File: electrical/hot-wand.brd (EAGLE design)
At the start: 112 x 72 mm, 188 parts, among them IC1 12V R-78K12-2.0, IC2 3V3 R-78K3.3, Q1 STP19NF20, Q2 IRF510, Q3 BC846B, Q4 SIRS5800DP-T1-GE3, Q5 2N7002K, Q6 DMTH64M2LPDWQ-13, Q7 G3404, U1 TPS54560DDA, U2 1EDN8511BXUSA1, U3 INA138, U4 LM74700QDBVTQ1, U5 AP53781, U6 SSD1306-4PIN-0.91N-VERT, U7 STM32F030F4P6, Y1 27.12 MHz 10pF

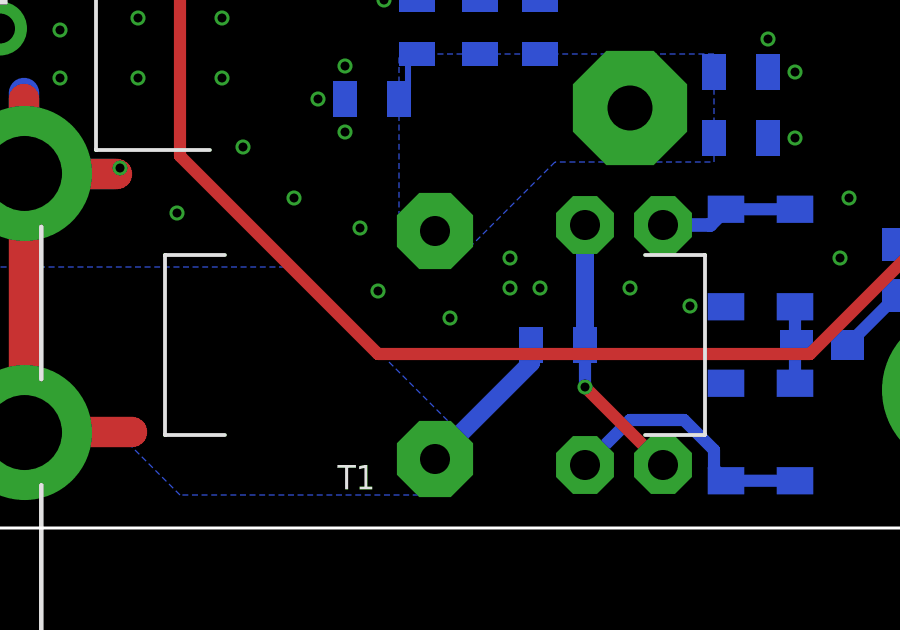
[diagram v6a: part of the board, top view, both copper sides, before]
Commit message: more work regarding current transformer, better diode bom
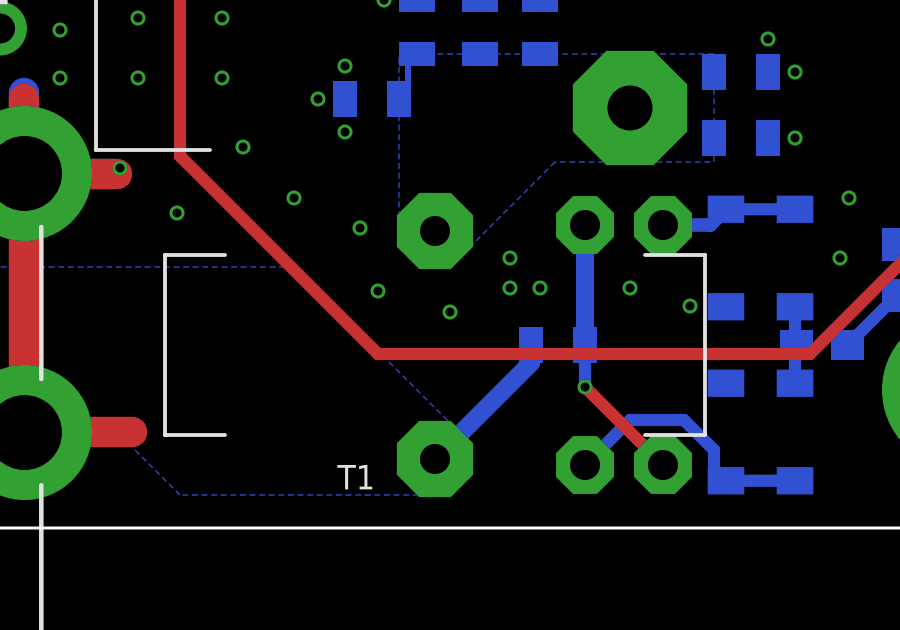
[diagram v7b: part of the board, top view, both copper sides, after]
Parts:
- D7: value 4148 -> 1N4148W
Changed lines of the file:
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@@
 <attribute name="JLC-DNP" value="2" x="90.6" y="6.1" size="1.778" layer="28" rot="MR180" display="off"/>
 </element>
-<element name="D7" library="hot-wand" package="SOD123FL" value="4148" x="96.2" y="3.2" smashed="yes" rot="MR90">
+<element name="D7" library="hot-wand" package="SOD123FL" value="1N4148W" x="96.2" y="3.2" smashed="yes" rot="MR90">
 <attribute name="NAME" x="95.2" y="5.5" size="0.8128" layer="26" font="vector" rot="MR270"/>
-<attribute name="JLCPARTNUM" value="C917030" x="96.2" y="3.2" size="1.778" layer="28" rot="MR90" display="off"/>
+<attribute name="JLCPARTNUM" value="C84367" x="96.2" y="3.2" size="1.778" layer="28" rot="MR90" display="off"/>
 </element>
 <element name="D5" library="hot-wand" package="SOD123FL" value="4148" x="98.5" y="3.2" smashed="yes" rot="MR270">
 <attribute name="NAME" x="99.5" y="1" size="0.8128" layer="26" font="vector" rot="MR90"/>
-<attribute name="JLCPARTNUM" value="C917030" x="98.5" y="3.2" size="1.778" layer="28" rot="MR270" display="off"/>
+<attribute name="JLCPARTNUM" value="C84367" x="98.5" y="3.2" size="1.778" layer="28" rot="MR270" display="off"/>
 </element>
 <element name="D6" library="hot-wand" package="SOD123FL" value="4148" x="98.5" y="9" smashed="yes" rot="MR270">
 <attribute name="NAME" x="95.2" y="9.1" size="0.8128" layer="26" font="vector" rot="MR270"/>
-<attribute name="JLCPARTNUM" value="C917030" x="98.5" y="9" size="1.778" layer="28" rot="MR270" display="off"/>
+<attribute name="JLCPARTNUM" value="C84367" x="98.5" y="9" size="1.778" layer="28" rot="MR270" display="off"/>
 </element>
 <element name="D8" library="hot-wand" package="SOD123FL" value="4148" x="96.2" y="9" smashed="yes" rot="MR90">
 <attribute name="NAME" x="99.4" y="7.4" size="0.8128" layer="26" font="vector" rot="MR90"/>
-<attribute name="JLCPARTNUM" value="C917030" x="96.2" y="9" size="1.778" layer="28" rot="MR90" display="off"/>
+<attribute name="JLCPARTNUM" value="C84367" x="96.2" y="9" size="1.778" layer="28" rot="MR90" display="off"/>
 </element>
 <element name="R10" library="hot-wand" package="0603-RES" value="100Ω" x="99.4" y="6.1" smashed="yes" rot="MR180">
@@
 <via x="89" y="8" extent="1-16" drill="0.3" shape="octagon"/>
 <via x="89" y="9" extent="1-16" drill="0.3" shape="octagon"/>
-<via x="87" y="7" extent="1-16" drill="0.3" shape="octagon"/>
+<via x="87" y="7.2" extent="1-16" drill="0.3" shape="octagon"/>
 <via x="84" y="10" extent="1-16" drill="0.3" shape="octagon"/>
 <via x="32.4" y="52.8" extent="1-16" drill="0.3" shape="octagon"/>

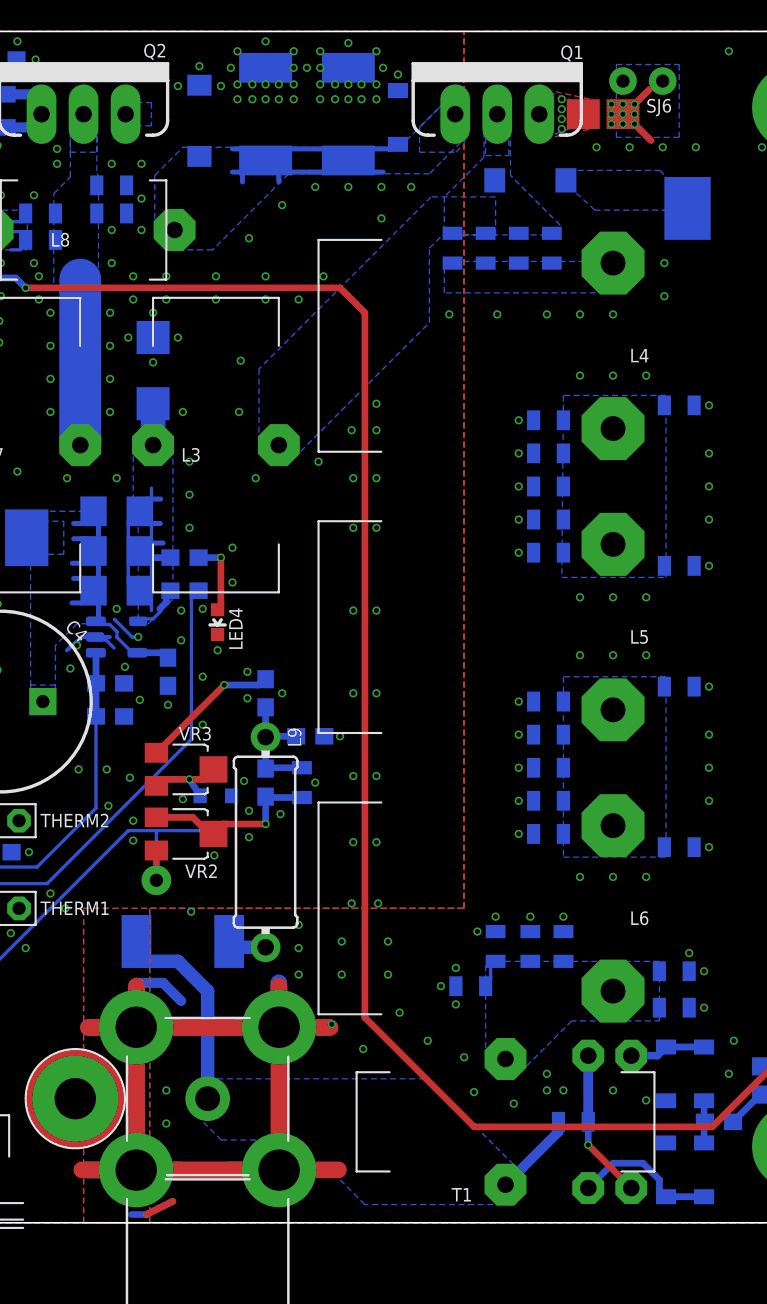
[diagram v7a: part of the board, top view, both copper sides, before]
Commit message: another hole for the air core inductor, moved a diode
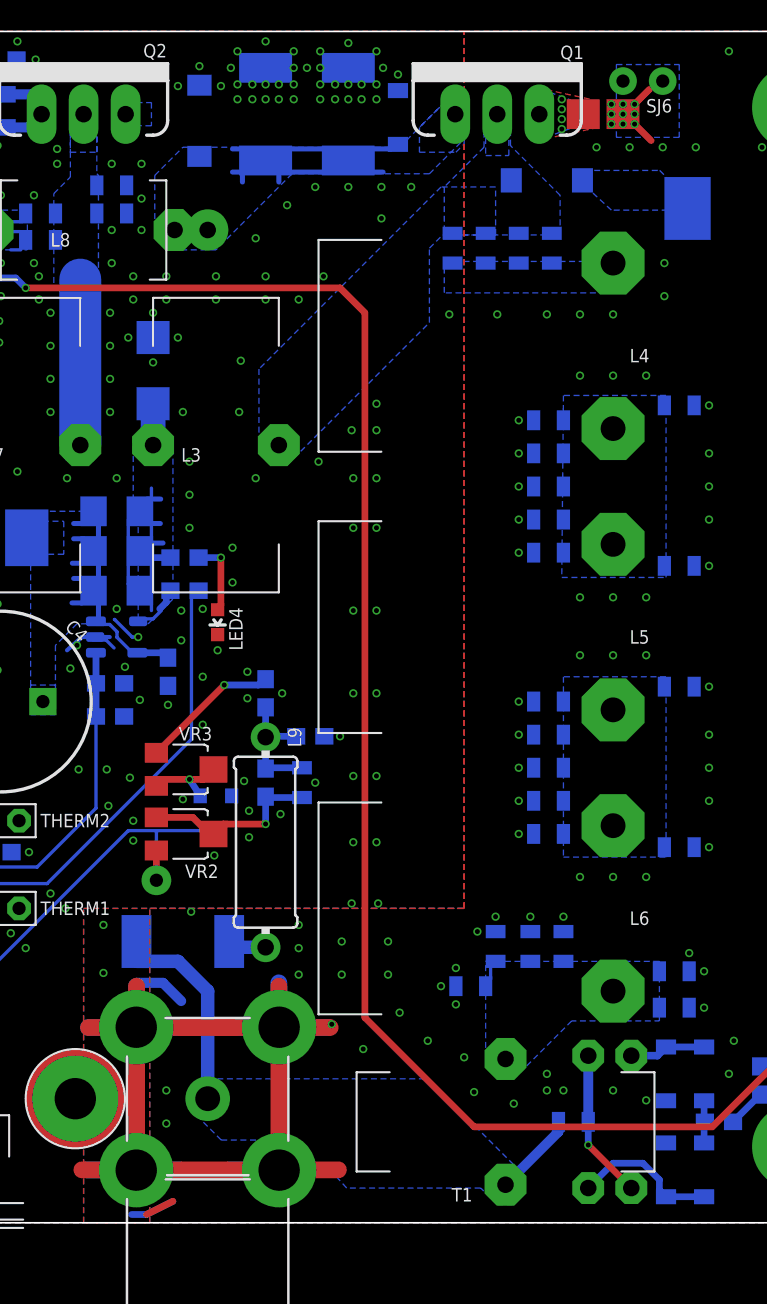
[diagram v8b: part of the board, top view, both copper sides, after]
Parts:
- moved D4 1.00 mm to (89.0, 63.0)
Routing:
- net RF-GATE: vias 0 -> 1
- net GND: vias 652 -> 654
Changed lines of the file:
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@@
 <attribute name="PARTNUM" value="CHV0805N250104KXT;MBASQ21GAB7104KTCA01;MBASQ21GAB7104MTCA01" x="83.3" y="58.9" size="1.778" layer="28" rot="MR270" display="off"/>
 </element>
-<element name="D4" library="hot-wand" package="SMA-DIODE" value="ES1J" x="88" y="63" smashed="yes" rot="MR180">
-<attribute name="NAME" x="84.886" y="62.951" size="0.8128" layer="26" font="vector" rot="MR0"/>
-<attribute name="VALUE" x="84.946" y="61.951" size="0.8128" layer="28" font="vector" rot="MR0"/>
-<attribute name="JLCPARTNUM" value="C64879" x="88" y="63" size="1.778" layer="28" rot="MR180" display="off"/>
-<attribute name="JLC_ROTATION" value="180" x="88" y="63" size="1.778" layer="28" rot="MR180" display="off"/>
+<element name="D4" library="hot-wand" package="SMA-DIODE" value="ES1J" x="89" y="63" smashed="yes" rot="MR180">
+<attribute name="NAME" x="85.886" y="62.951" size="0.8128" layer="26" font="vector" rot="MR0"/>
+<attribute name="VALUE" x="85.946" y="61.951" size="0.8128" layer="28" font="vector" rot="MR0"/>
+<attribute name="JLCPARTNUM" value="C64879" x="89" y="63" size="1.778" layer="28" rot="MR180" display="off"/>
+<attribute name="JLC_ROTATION" value="180" x="89" y="63" size="1.778" layer="28" rot="MR180" display="off"/>
 </element>
 <element name="TVS1" library="hot-wand" package="SMC" value="SM15T150CA" x="101.2" y="61.3" smashed="yes" rot="MR180">
@@
 <via x="77" y="62.6" extent="1-16" drill="0.3" shape="octagon"/>
 <via x="75" y="62.6" extent="1-16" drill="0.3" shape="octagon"/>
-<via x="73" y="61.5" extent="1-16" drill="0.3" shape="octagon"/>
-<via x="71" y="59.5" extent="1-16" drill="0.3" shape="octagon"/>
+<via x="73.3" y="61.5" extent="1-16" drill="0.3" shape="octagon"/>
+<via x="71.4" y="59.5" extent="1-16" drill="0.3" shape="octagon"/>
 <via x="29" y="7.4" extent="1-16" drill="0.3" shape="octagon"/>
 <polygon width="0.2032" layer="16" spacing="0.2032" isolate="0.2032" thermals="no">
@@
 <wire x1="64.2" y1="14.5" x2="65.8" y2="14.5" width="0.6096" layer="16"/>
 <wire x1="65.8" y1="14.5" x2="66.9" y2="13.4" width="0.6096" layer="16"/>
+<via x="62.2" y="15.1" extent="1-16" drill="0.3" shape="octagon"/>
+<via x="62.2" y="18" extent="1-16" drill="0.3" shape="octagon"/>
 </signal>
 <signal name="RF-OUT">
@@
 <vertex x="87.7" y="1.881021875"/>
 <vertex x="86.918978125" y="1.1"/>
-<vertex x="78" y="1.1"/>
+<vertex x="86" y="1.1"/>
+<vertex x="85" y="2.1"/>
+<vertex x="76.9" y="2.1"/>
 </polygon>
 <wire x1="86.5" y1="2.3" x2="89.7" y2="5.5" width="0.6" layer="16"/>
@@
 <polygon width="0.2032" layer="16" spacing="0.2032" isolate="0.8" rank="2">
 <vertex x="85.2" y="67.1"/>
-<vertex x="85.2" y="64.4"/>
-<vertex x="82.8" y="62"/>
+<vertex x="85.2" y="65"/>
+<vertex x="82.8" y="62.6"/>
 <vertex x="82.8" y="59.7"/>
 <vertex x="89.8" y="59.7"/>
-<vertex x="89.8" y="60.3"/>
-<vertex x="86.8" y="63.3"/>
+<vertex x="89.8" y="62.1"/>
+<vertex x="86.8" y="65.1"/>
 <vertex x="86.8" y="67.1"/>
 </polygon>
@@
 <vertex x="82.7" y="59.7"/>
 <vertex x="85.9" y="59.7"/>
-<vertex x="85.9" y="62"/>
-<vertex x="82" y="62"/>
+<vertex x="85.9" y="62.6"/>
+<vertex x="82.6" y="62.6"/>
 <vertex x="71.6" y="51.6"/>
 <vertex x="71.6" y="46.5"/>
@@
 <polygon width="0.2032" layer="16" spacing="0.2032" isolate="0.8" thermals="no" rank="2">
 <vertex x="96.3" y="61.2"/>
-<vertex x="91.9" y="61.2"/>
-<vertex x="90.6" y="62.4"/>
-<vertex x="89.7" y="62.4"/>
-<vertex x="89.7" y="63.6"/>
+<vertex x="92.9" y="61.2"/>
+<vertex x="91.6" y="62.4"/>
+<vertex x="90.7" y="62.4"/>
+<vertex x="90.7" y="63.6"/>
 <vertex x="95.817159375" y="63.6"/>
 <vertex x="96.3" y="63.117159375"/>
@@
 <vertex x="65.3" y="63.3"/>
 <vertex x="67" y="65"/>
-<vertex x="68.4" y="65"/>
 <vertex x="80.1" y="65"/>
-<vertex x="80.9" y="65.8"/>
 <vertex x="83" y="67.9"/>
 <vertex x="84.2" y="67.9"/>
 <vertex x="84.2" y="65.7"/>
-<vertex x="82.6" y="64.1"/>
 <vertex x="81.9" y="63.4"/>
-<vertex x="73.4" y="63.4"/>
-<vertex x="68.8" y="58.8"/>
+<vertex x="73.6" y="63.4"/>
+<vertex x="69" y="58.8"/>
 <vertex x="66" y="58.8"/>
 </polygon>
@@
 <wire x1="72.8" y1="63.4" x2="72.8" y2="62.9" width="0.3048" layer="16"/>
 <wire x1="70.6" y1="63.4" x2="70.6" y2="62.9" width="0.3048" layer="16"/>
+<via x="68.5" y="60" extent="1-16" drill="1" diameter="2.5" shape="octagon" alwaysstop="yes"/>
 </signal>
 <signal name="N$14">
